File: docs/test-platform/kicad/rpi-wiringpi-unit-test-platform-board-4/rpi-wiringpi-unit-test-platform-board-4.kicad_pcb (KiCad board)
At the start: 2 copper layers, 9 parts, among them J1 JST_IN_PWR, J2 JST_IN_I2C, M1 DS3231_0x68+AT24C32_0x57, M2 BMP180_0x77, M3 SSD1306_0x3c, SW1 SW_DIP_x01

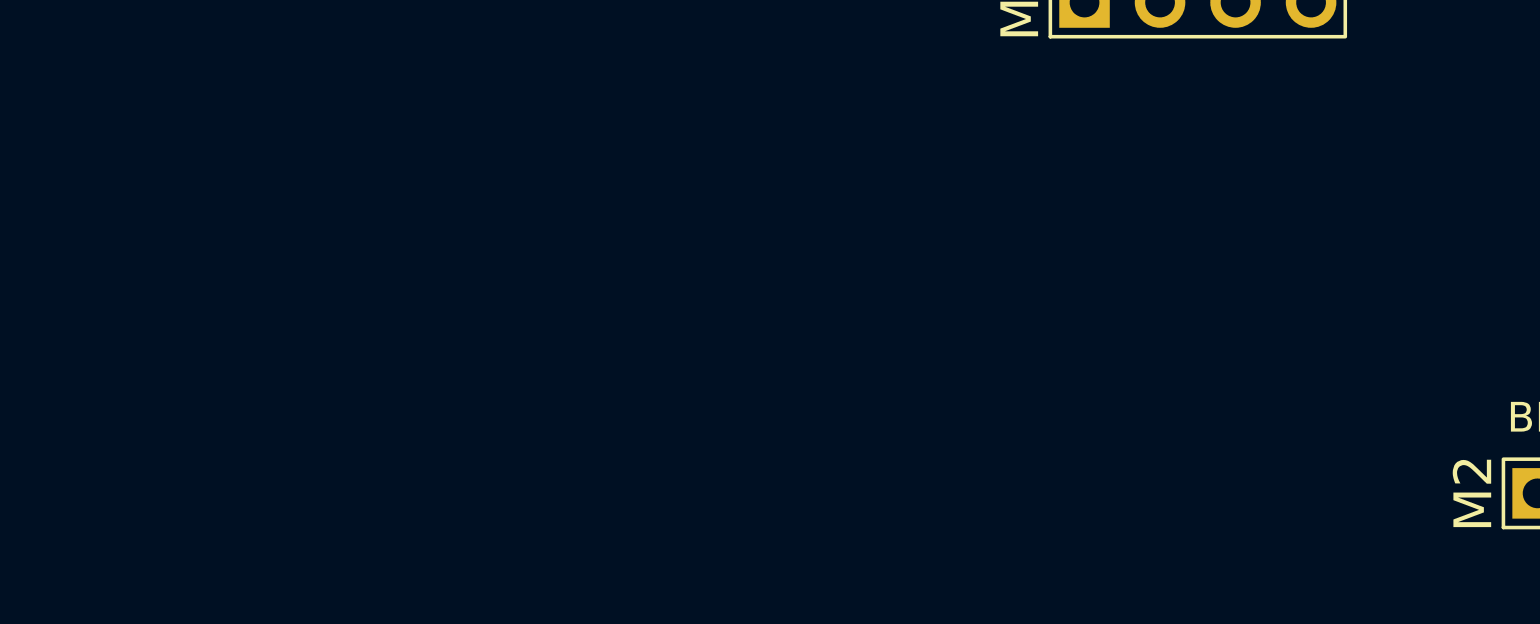
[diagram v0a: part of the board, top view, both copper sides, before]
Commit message: Add ability to dynamically configure board revision number
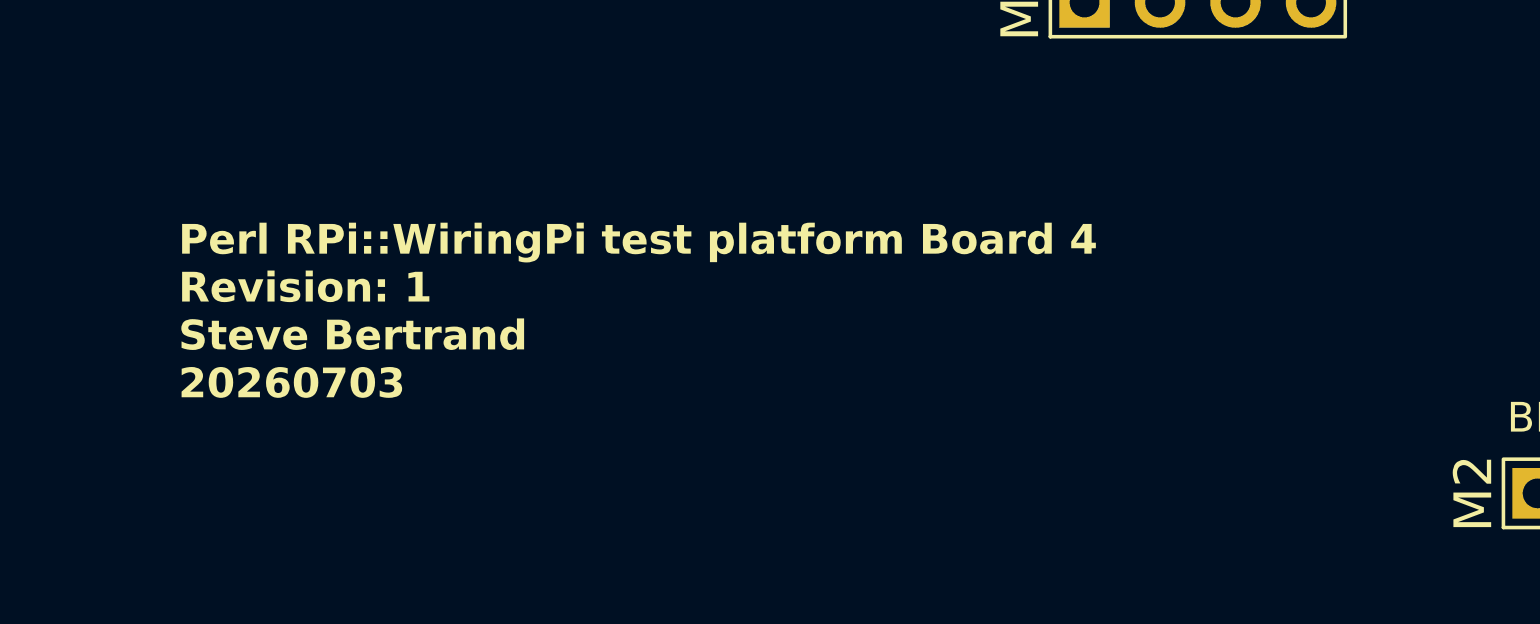
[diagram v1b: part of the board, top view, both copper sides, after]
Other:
- board text added: "Perl RPi::WiringPi test platform Board 4 Revision: ${REVISION} Steve Bertrand 20260703"
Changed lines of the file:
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@@
 	)
 	(paper "A4")
+	(title_block
+		(date "2026-07-03")
+		(rev "1")
+	)
 	(layers
 		(0 "F.Cu" signal)
@@
 			)
 			(justify left bottom)
+		)
+	)
+	(gr_text "Perl RPi::WiringPi test platform Board 4\nRevision: ${REVISION}\nSteve Bertrand\n20260703"
+		(at 142.24 115 0)
+		(layer "F.SilkS")
+		(effects
+			(font
+				(size 1 1)
+				(thickness 0.2)
+				(bold yes)
+			)
+			(justify left bottom)

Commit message: Finalize board 4 hardware
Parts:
- removed J1: JST_IN_PWR, rpi-wiringpi-unit-test-platform-board-4:J1
- removed J2: JST_IN_I2C, rpi-wiringpi-unit-test-platform-board-4:J2
- removed M3: SSD1306_0x3c, rpi-wiringpi-unit-test-platform-board-4:M3
- added J3: JST_IN, Connector_JST:JST_XH_B5B-XH-A_1x05_P2.50mm_Vertical, F.Cu at (131.7, 125.9)
- added OLED1: SSD1306_128_64, RPi:OLED_SSD_1306_128_64, F.Cu at (167.4, 103.4)
- added REF**: MountingHole_2.2mm_M2, MountingHole:MountingHole_2.2mm_M2, F.Cu at (91.3, 132.8)
- added REF**: MountingHole_2.2mm_M2, MountingHole:MountingHole_2.2mm_M2, F.Cu at (183.6, 132.8)
- added REF**: 2.2mm_M2, MountingHole:MountingHole_2.2mm_M2, F.Cu at (183.6, 87.2)
- added REF**: MountingHole_2.2mm_M2, MountingHole:MountingHole_2.2mm_M2, F.Cu at (91.3, 87.2)
- M1: footprint rpi-wiringpi-unit-test-platform-board-4:M1 -> RPi:DS3231
- M2: value BMP180_0x77 -> BMP180; footprint rpi-wiringpi-unit-test-platform-board-4:M2 -> RPi:BMP180
- SW1: value SW_DIP_x01 -> SW_LED_BRD_CONN; footprint rpi-wiringpi-unit-test-platform-board-4:SW1 -> Button_Switch_SMD:SW_DIP_SPSTx01_Slide_6.7x4.1mm_W6.73mm_P2.54mm_LowProfile_JPin
- moved R1 98.6 mm to (107.8, 117.1)
- moved C1 70.1 mm to (122.3, 126.4)
- moved M2 62.5 mm to (127.9, 100.7), turned to 180 degrees
- moved D1 52.6 mm to (143.0, 103.0)
- moved SW1 38.6 mm to (143.8, 93.2)
- moved M1 36.8 mm to (106.4, 91.8), turned to 0 degrees
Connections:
- M2 pad 1: +3V3 -> unconnected-(M2-VIN-Pad1)
- M2 pad 2: GND -> +3V3
- M2 pad 3: /I2C_SCL -> GND
- M2 pad 4: /I2C_SDA -> /I2C_SCL
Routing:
- net +3V3: track 0.00 -> 196.1 mm
- net /I2C_SDA: track 0.00 -> 115.7 mm
- net /I2C_SCL: track 0.00 -> 115.1 mm
- net Net-(D1-K): track 0.00 -> 34.4 mm
- net Net-(D1-A): track 0.00 -> 11.9 mm
- net GND: track 0.00 -> 11.2 mm, vias 0 -> 24
- added copper zone on B.Cu, net GND
- added copper zone on F.Cu, net GND
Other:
- board outline added: 98.2 x 51.9 mm
- board text added: "+3V3"
- board text added: "BRD_CONN"
- board text added: "GND"
- board text added: "I2C_SCL"
- board text added: "I2C_SDA"
- board text added: "OFF"
- board text added: "ON"
- board text added: "Perl RPi::WiringPi test platform Board 4 Revision: ${REVISION} Steve Bertrand 20260704"
- board text added: "RPI_BOARD_4"
- board text removed: "0x68 + 0x57"
- board text removed: "Perl RPi::WiringPi test platform Board 4 Revision: ${REVISION} Steve Bertrand 20260703"

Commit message: Finish boards
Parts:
- SW1: value SW_LED_BRD_CONN -> SW_DIP_x01
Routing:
- net /I2C_SDA: track 115.7 -> 116.3 mm
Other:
- board text added: "+"
- board text added: "-"

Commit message: Move cap closer to pins; cleanup
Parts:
- moved C1 11.6 mm to (131.8, 119.6)
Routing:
- net GND: track 11.2 -> 0.00 mm, vias 24 -> 25
- net +3V3: track 196.1 -> 188.5 mm
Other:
- board text added: "Perl RPi::WiringPi test platform Board 4 Revision: ${REVISION} Steve Bertrand ${CURRENT_DATE}"
- board text removed: "Perl RPi::WiringPi test platform Board 4 Revision: ${REVISION} Steve Bertrand 20260704"
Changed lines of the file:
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@@
 	(footprint "Capacitor_THT:CP_Radial_D5.0mm_P2.50mm"
 		(layer "F.Cu")
-		(at 122.341 126.365)
+		(at 131.826 119.634)
 		(descr "CP, Radial series, Radial, pin pitch=2.50mm, diameter=5mm, height=7mm, Electrolytic Capacitor")
 		(tags "CP Radial series Radial pin pitch 2.50mm diameter 5mm height 7mm Electrolytic Capacitor")
 		(property "Reference" "C1"
-			(at 1.25 -3.75 0)
+			(at 3.683 -2.921 0)
 			(layer "F.SilkS")
 			(effects
@@
 		)
 		(property "Value" "10µf"
-			(at 1.25 3.75 0)
+			(at 4.699 -0.254 90)
 			(layer "F.SilkS")
 			(effects
@@
 		(tags "connector JST XH vertical")
 		(property "Reference" "J3"
-			(at 5 -3.55 0)
+			(at -2.326 -3.683 0)
 			(layer "F.SilkS")
 			(effects
@@
 		)
 	)
-	(gr_text "Perl RPi::WiringPi test platform Board 4\nRevision: ${REVISION}\nSteve Bertrand\n20260704"
-		(at 120.396 118.237 0)
+	(gr_text "Perl RPi::WiringPi test platform Board 4\nRevision: ${REVISION}\nSteve Bertrand\n${CURRENT_DATE}"
+		(at 118.11 117.856 0)
 		(layer "F.SilkS")
 		(effects
@@
 	)
 	(gr_text "RPI_BOARD_4"
-		(at 155.956 128.524 0)
+		(at 151.003 133.096 0)
 		(layer "F.SilkS")
 		(effects
@@
 		)
 	)
-	(segment
-		(start 132.588 124.079)
-		(end 126.746 124.079)
-		(width 0.4)
-		(layer "F.Cu")
-		(net "GND")
-	)
-	(segment
-		(start 134.239 125.857)
-		(end 132.588 124.079)
-		(width 0.4)
-		(layer "F.Cu")
-		(net "GND")
-	)
-	(segment
-		(start 126.746 124.079)
-		(end 124.841 126.365)
-		(width 0.4)
-		(layer "F.Cu")
-		(net "GND")
-	)
 	(via
 		(at 160.782 107.95)
@@
 	)
 	(via
+		(at 134.366 127.889)
+		(size 0.8)
+		(drill 0.4)
+		(layers "F.Cu" "B.Cu")
+		(free yes)
+		(net "GND")
+	)
+	(via
 		(at 99.314 101.854)
 		(size 0.8)
@@
 		(layers "F.Cu" "B.Cu")
 		(net "GND")
-	)
-	(segment
-		(start 132.969 127.635)
-		(end 131.739 125.857)
-		(width 0.4)
-		(layer "F.Cu")
-		(net "+3V3")
 	)
 	(segment
@@
 	)
 	(segment
-		(start 125.603 132.207)
-		(end 120.65 132.207)
+		(start 131.739 120.102)
+		(end 131.739 125.857)
 		(width 0.4)
 		(layer "F.Cu")
@@
 	)
 	(segment
-		(start 130.302 125.857)
-		(end 127.381 128.778)
+		(start 131.739 125.857)
+		(end 109.855 125.857)
+		(width 0.4)
+		(layer "F.Cu")
+		(net "+3V3")
+	)
+	(segment
+		(start 131.826 119.634)
+		(end 131.826 120.015)
+		(width 0.4)
+		(layer "F.Cu")
+		(net "+3V3")
+	)
+	(segment
+		(start 133.096 129.032)
+		(end 131.739 125.857)
 		(width 0.4)
 		(layer "F.Cu")
@@
 	)
 	(segment
-		(start 131.739 125.857)
-		(end 130.302 125.857)
+		(start 131.826 120.015)
+		(end 131.739 120.102)
 		(width 0.4)
 		(layer "F.Cu")
@@
 	)
 	(segment
-		(start 131.739 125.857)
-		(end 125.603 132.207)
+		(start 135.763 129.032)
+		(end 133.096 129.032)
 		(width 0.4)
 		(layer "F.Cu")
@@
 	)
 	(segment
-		(start 122.341 126.786)
-		(end 124.333 128.778)
+		(start 136.739 125.857)
+		(end 135.763 129.032)
 		(width 0.4)
 		(layer "F.Cu")
@@
 	)
 	(segment
-		(start 135.89 127.635)
-		(end 132.969 127.635)
-		(width 0.4)
-		(layer "F.Cu")
-		(net "+3V3")
-	)
-	(segment
-		(start 122.341 126.365)
-		(end 122.341 126.786)
-		(width 0.4)
-		(layer "F.Cu")
-		(net "+3V3")
-	)
-	(segment
-		(start 120.65 132.207)
+		(start 109.828813 125.883187)
 		(end 102.621 121.671)
 		(width 0.4)
@@
 		(width 0.4)
 		(layer "F.Cu")
-		(net "+3V3")
-	)
-	(segment
-		(start 124.333 128.778)
-		(end 127.381 128.778)
-		(width 0.4)
-		(layer "F.Cu")
-		(net "+3V3")
-	)
-	(segment
-		(start 136.739 125.857)
-		(end 135.89 127.635)
-		(width 0.4)
-		(layer "F.Cu")

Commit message: Cleanup of PCBs/schematics
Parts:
- SW1: footprint Button_Switch_SMD:SW_DIP_SPSTx01_Slide_6.7x4.1mm_W6.73mm_P2.54mm_LowProfile_JPin -> Button_Switch_THT:SW_DIP_SPSTx01_Slide_9.78x4.72mm_W7.62mm_P2.54mm
- moved SW1 3.96 mm to (140.1, 94.5)
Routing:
- net +3V3: track 188.5 -> 192.8 mm
- net Net-(D1-A): track 11.9 -> 10.9 mm
- net GND: vias 25 -> 34
